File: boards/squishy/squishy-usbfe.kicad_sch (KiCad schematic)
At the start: 21 parts, among them J1 USB_C_Receptacle, U1 LFE5UM5G-45F-8BG381C, U13 HD3SS460, U14 TPD4E02B04DQA, U15 TPD4E02B04DQA, U17 USB3318, U3 CYPD3174-24, U4 SP3400-02UTG, X2 13MHz

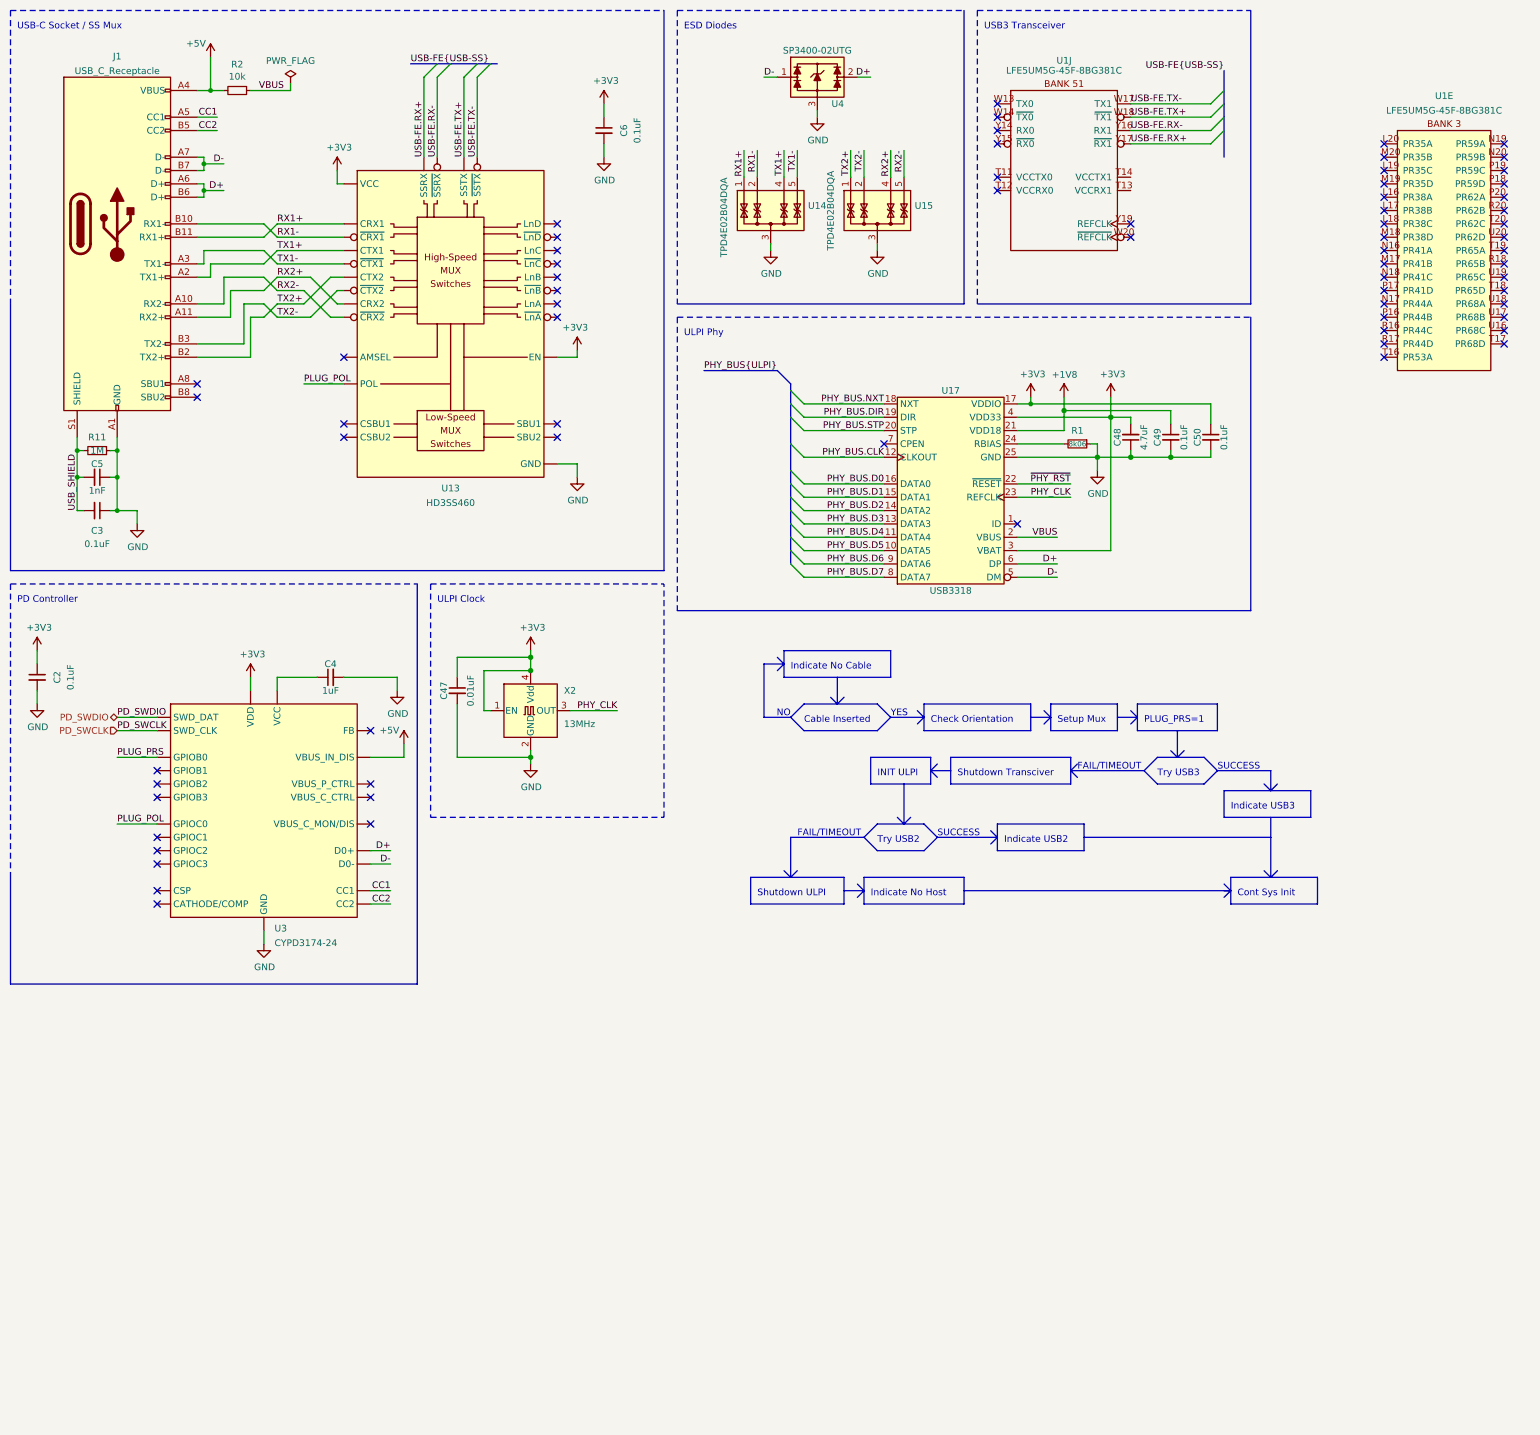
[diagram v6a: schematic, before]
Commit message: hardware: squishy: moved the flow diagram for the USB front-end bring-up
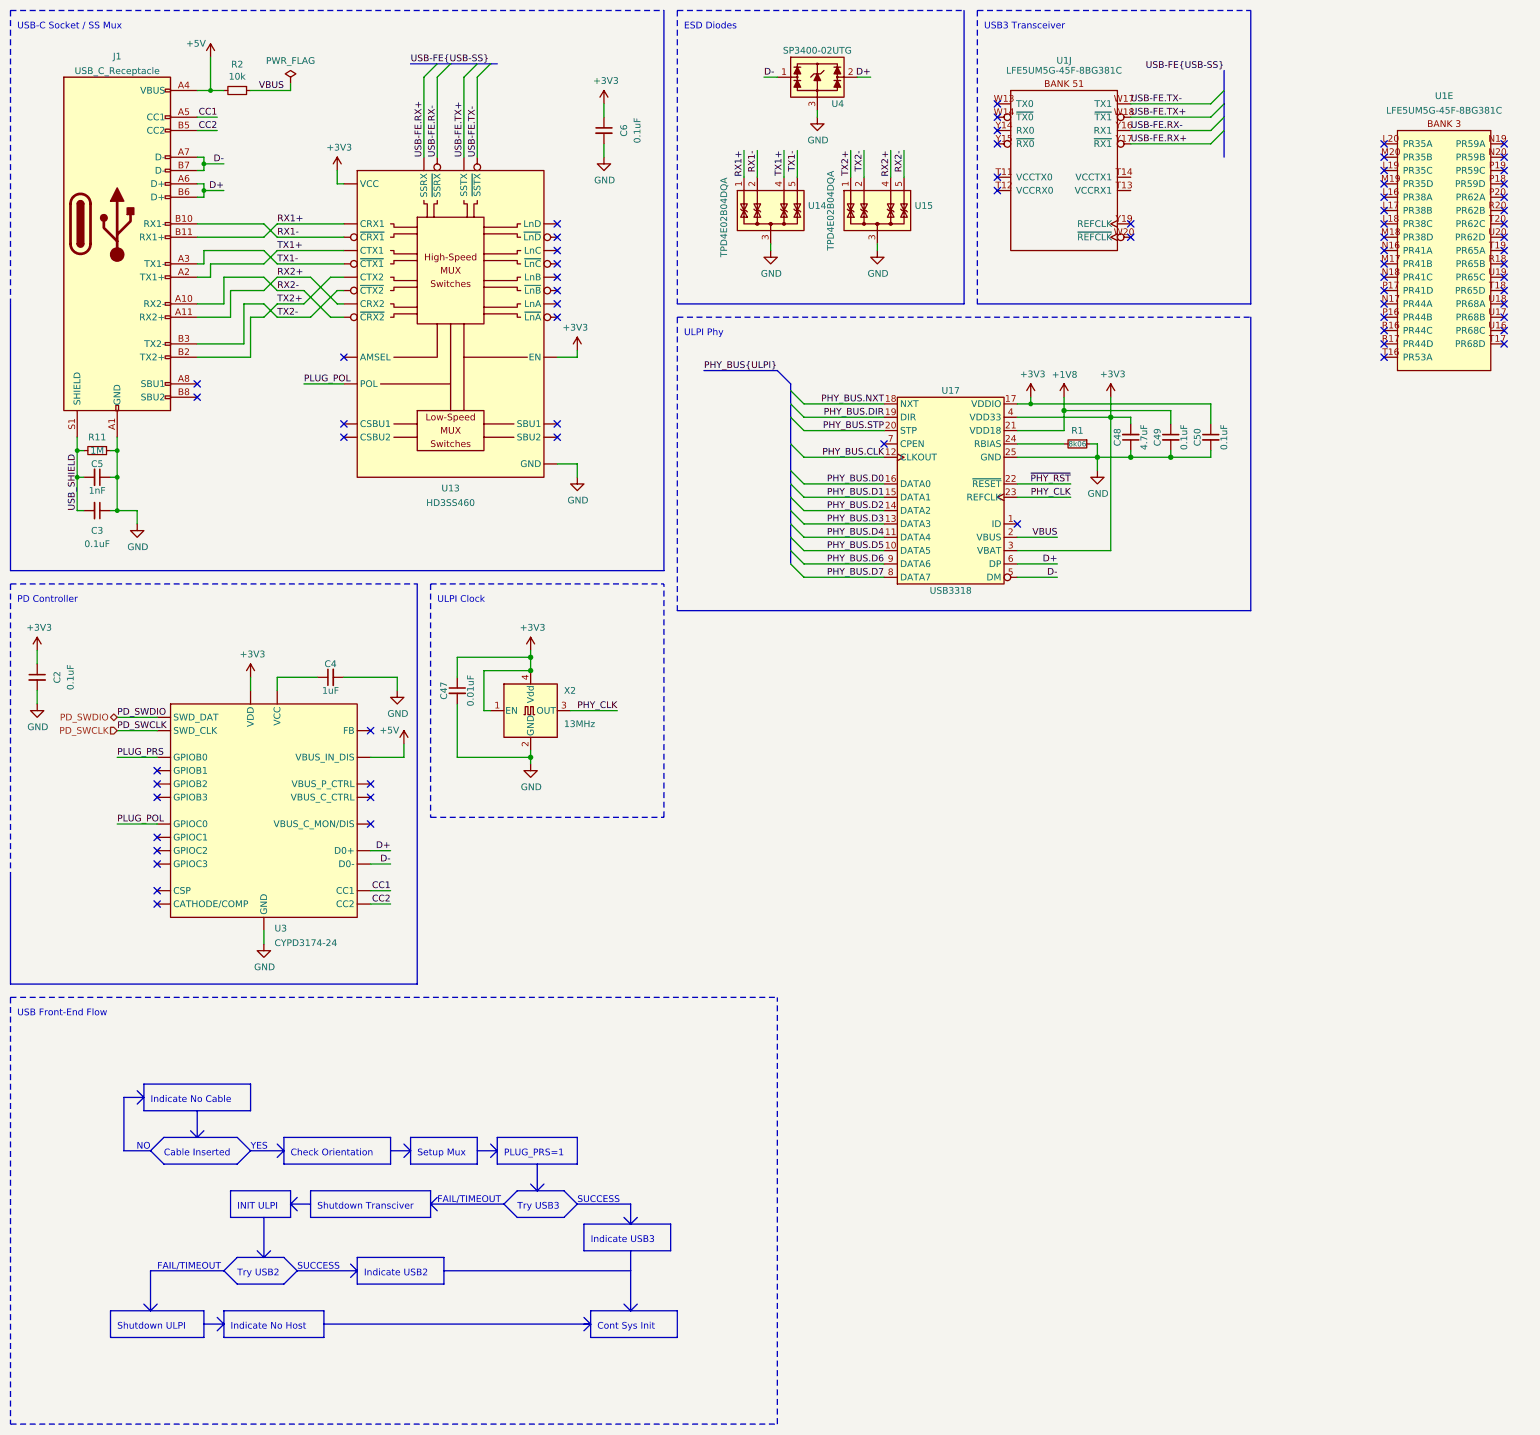
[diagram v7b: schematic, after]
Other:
- note added: "USB Front-End Flow"

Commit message: hardware: squishy: some minor ERC fixes
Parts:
- U14, U15: symbol DX-MON-NG:TPD4E02B04DQA -> DX-MON:TPD4E02B04DQA
- U4: symbol DX-MON-NG:SP3400-02UTG -> DX-MON:SP3400-02UTG
